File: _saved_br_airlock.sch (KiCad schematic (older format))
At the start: 19 parts, among them J1 RJ45_LEDS, J2 LEDS, J3 24v Power, J4 CONN_01X05, SW1 Door Release, SW2 SW_Reed, U1 PCF8574

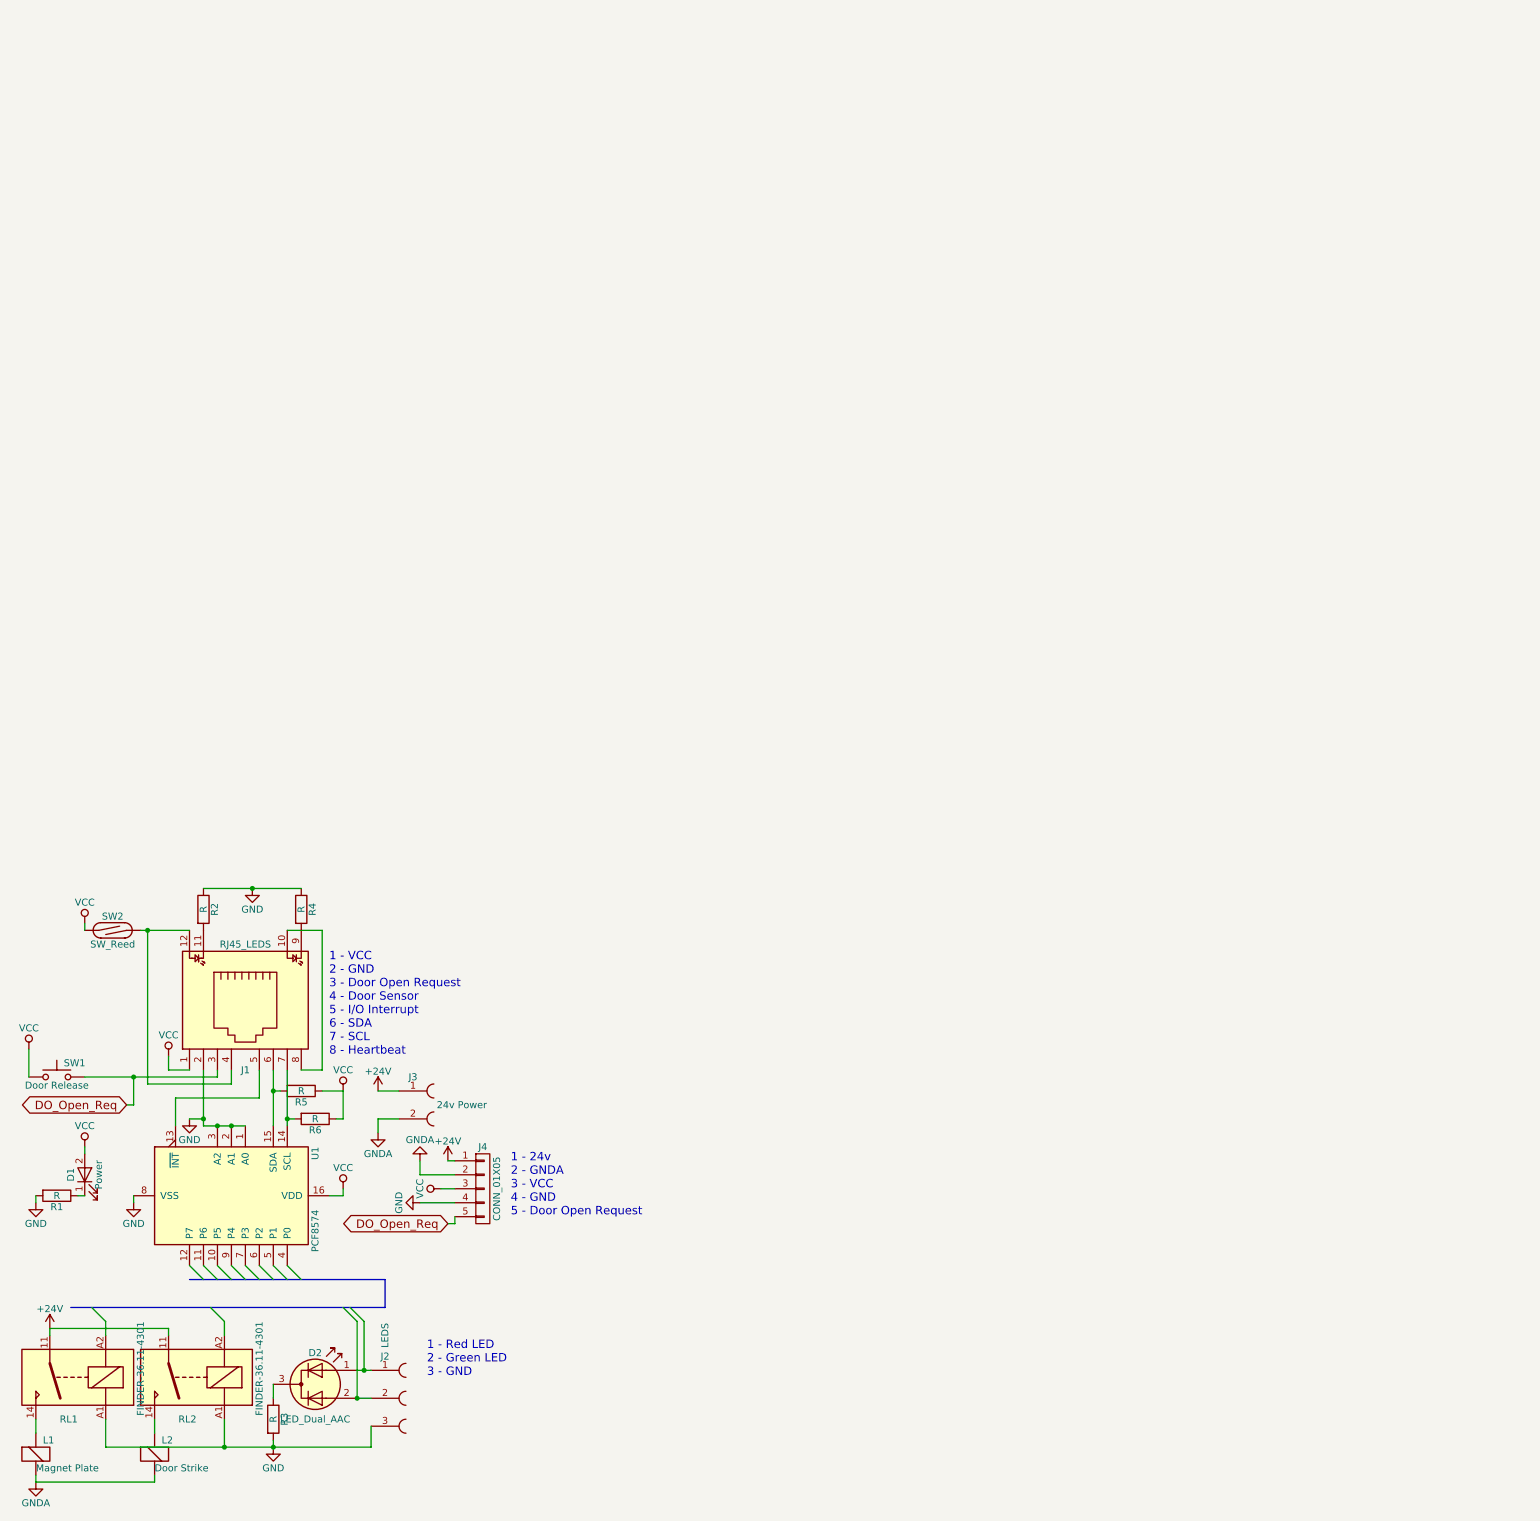
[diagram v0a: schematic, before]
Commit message: More work. Relay needs looking at, and a VERY rough visualisation of a PCB
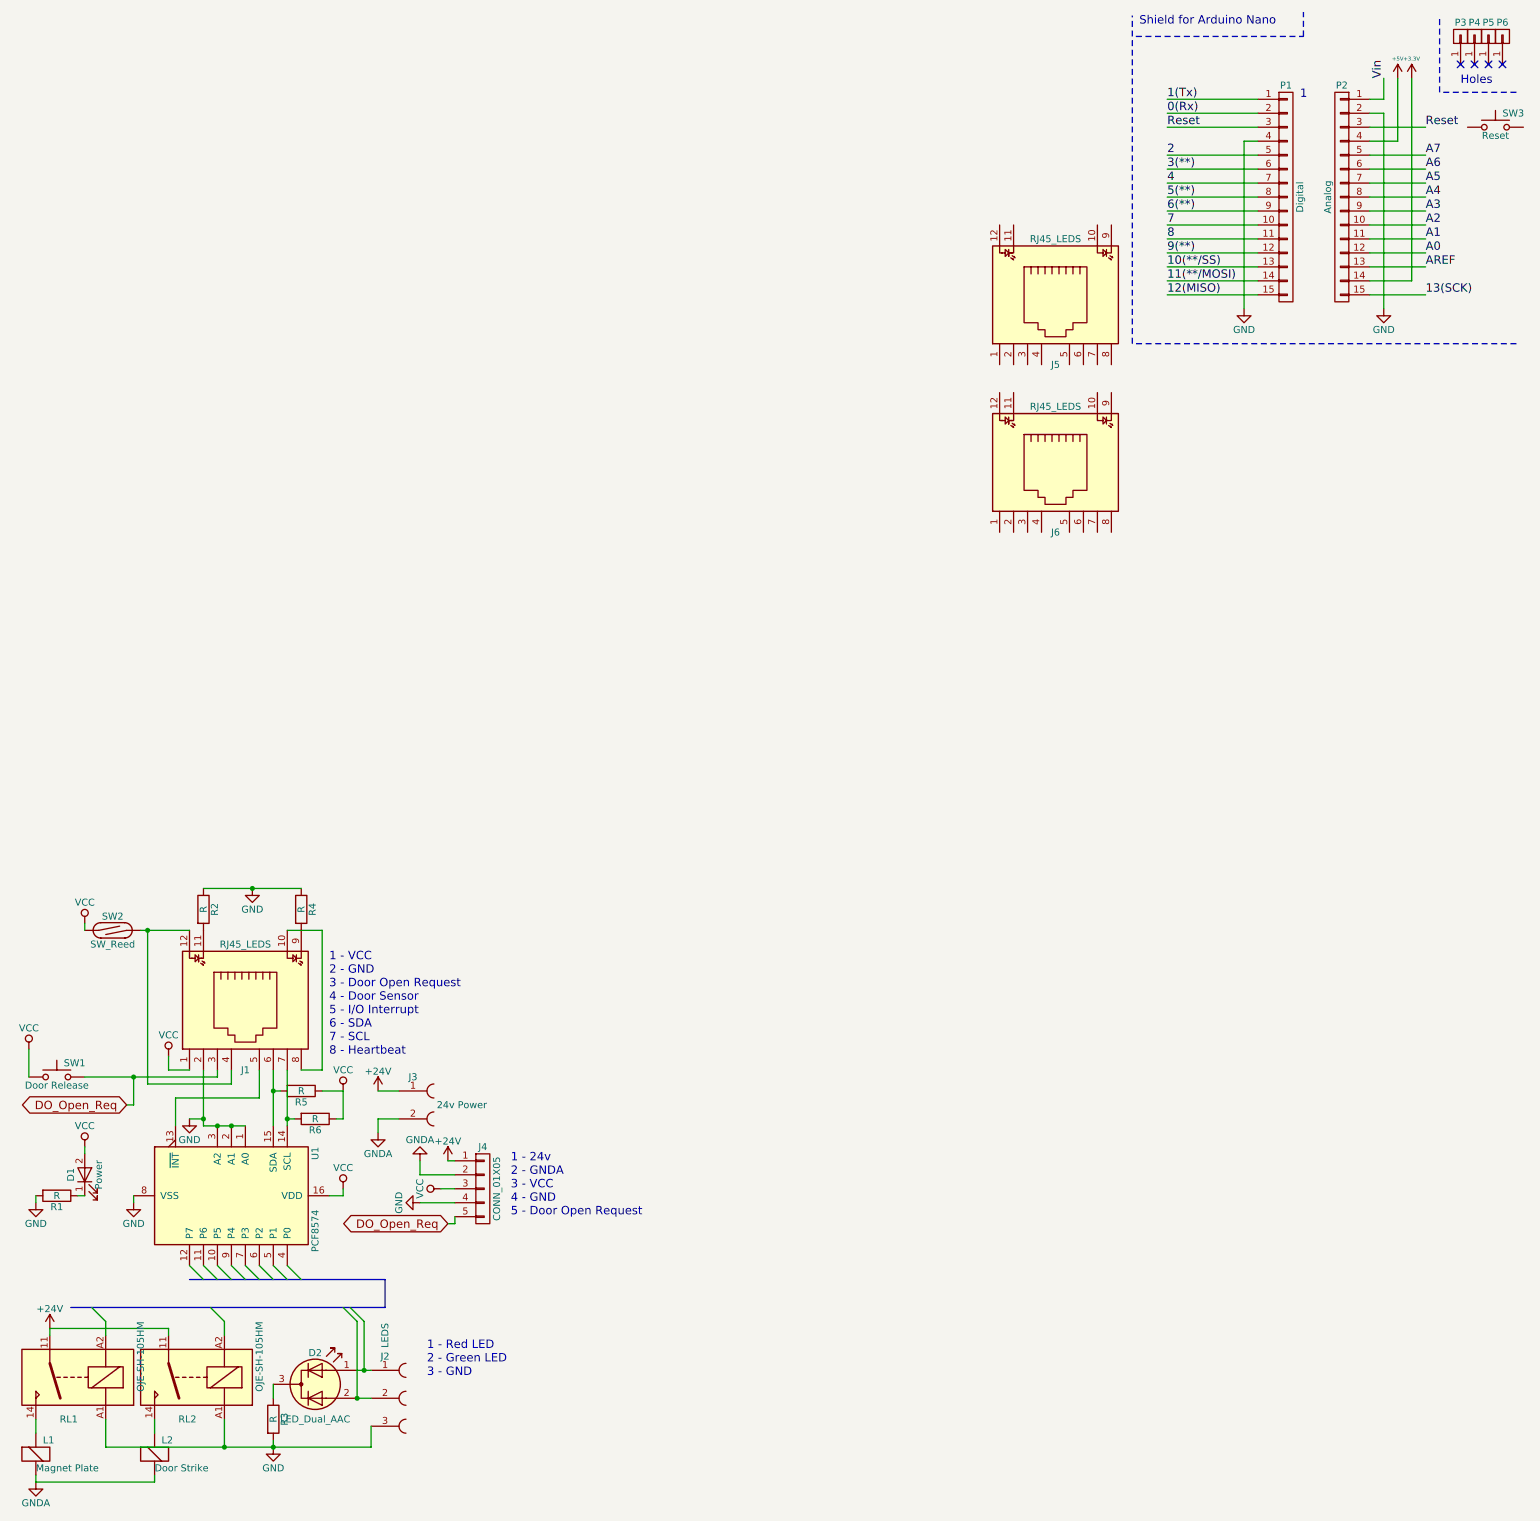
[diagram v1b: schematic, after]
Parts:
- added J5, J6: RJ45_LEDS, Connectors:RJ45_8, symbol RJ45_LEDS
- added P1: Digital, Socket_Arduino_Nano:Socket_Strip_Arduino_1x15, symbol CONN_01X15
- added P2: Analog, Socket_Arduino_Nano:Socket_Strip_Arduino_1x15, symbol CONN_01X15
- added P3, P4, P5, P6: CONN_01X01, Socket_Arduino_Nano:1pin_Nano, symbol CONN_01X01
- added SW3: Reset, Buttons_Switches_THT:SW_PUSH, symbol SW_Push
- RL1, RL2: value FINDER-36.11-4301 -> OJE-SH-105HM
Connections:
- net GND: now also P1.4 (P4), P2.2 (P2)
- new net +3V3: P2.14 (P14)
- new net +5V: P2.4 (P4)
- new net 0(Rx): P1.2 (P2)
- new net 1(Tx): P1.1 (P1)
- new net 10(**/SS): P1.13 (P13)
- new net 11(**/MOSI): P1.14 (P14)
- new net 12(MISO): P1.15 (P15)
- new net 13(SCK): P2.15 (P15)
- new net 2: P1.5 (P5)
- new net 3(**): P1.6 (P6)
- new net 4: P1.7 (P7)
- new net 5(**): P1.8 (P8)
- new net 6(**): P1.9 (P9)
- new net 7: P1.10 (P10)
- new net 8: P1.11 (P11)
- new net 9(**): P1.12 (P12)
- new net A0: P2.12 (P12)
- new net A1: P2.11 (P11)
- new net A2: P2.10 (P10)
- new net A3: P2.9 (P9)
- new net A4: P2.8 (P8)
- new net A5: P2.7 (P7)
- new net A6: P2.6 (P6)
- new net A7: P2.5 (P5)
- new net AREF: P2.13 (P13)
- new net Reset: P1.3 (P3), P2.3 (P3)
- new net Vin: P2.1 (P1)
- no-connect marks 0 -> 4
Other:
- note added: "1"
- note added: "Holes"
- note added: "Shield for Arduino Nano"
